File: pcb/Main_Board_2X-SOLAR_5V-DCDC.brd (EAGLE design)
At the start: 77.1 x 38.9 mm, 74 parts, among them CN5 USBA_FEMALE, M3AB FDMC8030, T2 MMUN2133LT1G, U1 LTC4015EUHFPBFQFN-38_UHF-M, U3 TPS61090RSAR, X1 6V_PV

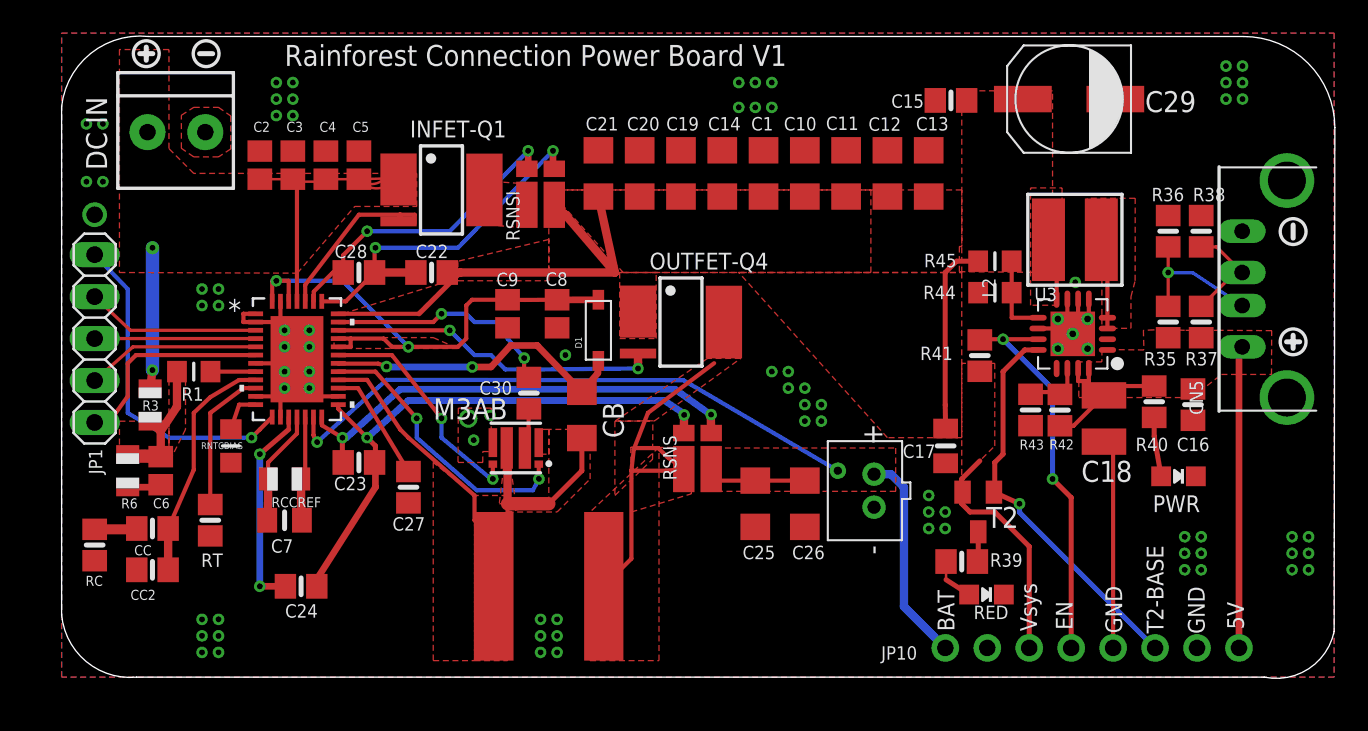
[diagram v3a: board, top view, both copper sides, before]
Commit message: Updated schematic and board layout for V1
Added jumper for VIN and updated footprint for 8030 package
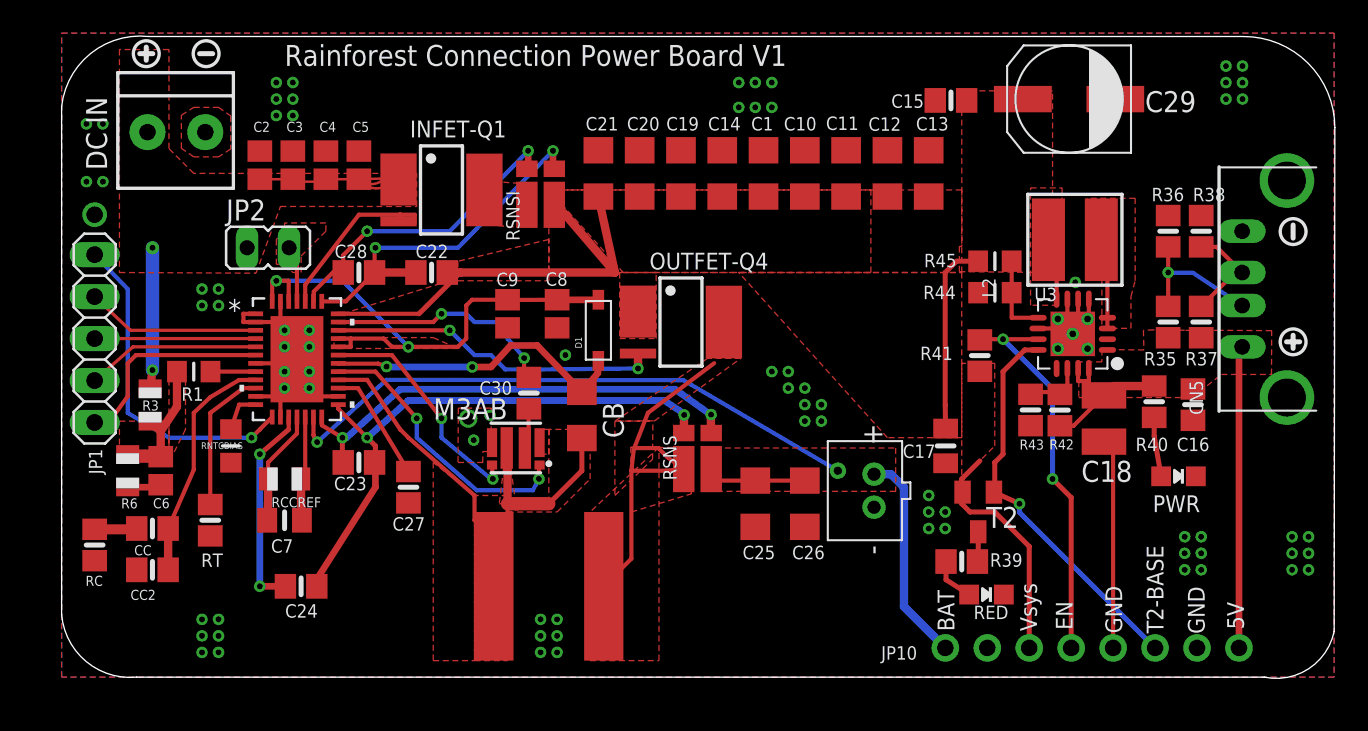
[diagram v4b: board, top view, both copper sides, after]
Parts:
- added JP2: (no value), jumper:JP1
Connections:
- new net N$12: JP2.2, U1.35
- net VIN: now also JP2.1; no longer U1.35
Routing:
- net VIN: track 29.1 -> 21.9 mm
- net N$12: track 0.00 -> 3.45 mm
- added copper zone on layer 1, net N$12
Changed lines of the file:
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@@
 <attribute name="PRICE" value="0.98 USD" x="23" y="29.5" size="1.778" layer="27" rot="R270" display="off"/>
 </element>
+<element name="JP2" library="jumper" library_urn="urn:adsk.eagle:library:252" package="JP1" package3d_urn="urn:adsk.eagle:package:15455/1" value="" x="12.5" y="26" rot="R270"/>
 </elements>
 <signals>
@@
 <wire x1="63.080540625" y1="17.028540625" x2="63.112" y2="17.06" width="0.254" layer="1"/>
 <wire x1="63.112" y1="17.06" x2="63.678" y2="17.626" width="0.254" layer="1"/>
-<wire x1="66.152" y1="17.626" x2="63.678" y2="17.626" width="0.254" layer="1"/>
+<wire x1="66.152" y1="17.626" x2="63.678" y2="17.626" width="0.508" layer="1"/>
 <wire x1="62.196" y1="17.927328125" x2="62.196" y2="18.686" width="0.254" layer="1"/>
 <wire x1="62.196" y1="17.927328125" x2="62.196" y2="17.028540625" width="0.254" layer="1"/>
@@
 <contactref element="C4" pad="1"/>
 <contactref element="C5" pad="1"/>
-<contactref element="U1" pad="35"/>
 <contactref element="X1" pad="1"/>
 <contactref element="R3" pad="2"/>
@@
 <vertex x="3.5" y="38"/>
 <vertex x="3.5" y="24.5"/>
-<vertex x="14.27" y="24.46"/>
-<vertex x="17.75" y="28.5"/>
+<vertex x="11.77" y="24.46"/>
+<vertex x="13.25" y="28.5"/>
 <vertex x="21.5" y="28.5"/>
 <vertex x="21.5" y="30.5"/>
@@
 <vertex x="6.5" y="32"/>
 </polygon>
-<wire x1="14.25" y1="22.7532" x2="14.25" y2="29.9" width="0.254" layer="1"/>
 <wire x1="14.425" y1="30.075" x2="14.25" y2="29.9" width="0.254" layer="1"/>
 <wire x1="19.541975" y1="30.191975" x2="18" y2="30.15" width="0.1524" layer="1"/>
@@
 <wire x1="5.5" y1="18.59" x2="5.36" y2="17.48" width="0.508" layer="1"/>
 <contactref element="INFET-Q1" pad="1-3"/>
+<contactref element="JP2" pad="1"/>
 </signal>
 <signal name="SYS">
@@
 <via x="28.9" y="12" extent="1-16" drill="0.35"/>
 <wire x1="28.9" y1="12" x2="28.89" y2="12.39" width="0.254" layer="1"/>
-<wire x1="28.89" y1="12.39" x2="28.89" y2="12.8971" width="0.254" layer="1"/>
+<wire x1="28.89" y1="12.39" x2="28.94" y2="12.845" width="0.254" layer="1"/>
 <wire x1="16.7532" y1="18.5" x2="19" y2="18.5" width="0.254" layer="1"/>
 <wire x1="19" y1="18.5" x2="21.5" y2="15.67" width="0.254" layer="1"/>
@@
 <contactref element="M3AB" pad="8"/>
 <via x="26.11" y="12" extent="1-16" drill="0.35"/>
-<wire x1="26.11" y1="12.8971" x2="26.11" y2="12" width="0.254" layer="1"/>
+<wire x1="26.06" y1="12.845" x2="26.11" y2="12" width="0.254" layer="1"/>
 <wire x1="16.7532" y1="19.5" x2="20" y2="19.5" width="0.254" layer="1"/>
 <wire x1="20" y1="19.5" x2="23" y2="15.67" width="0.254" layer="1"/>
@@
 <contactref element="R38" pad="1"/>
 <contactref element="CN5" pad="D+"/>
-<wire x1="69" y1="22.45" x2="71.05" y2="24.5" width="0.2" layer="1"/>
-<wire x1="71.05" y1="24.5" x2="71.48" y2="24.5" width="0.2" layer="1"/>
-<wire x1="71.48" y1="24.5" x2="69.93" y2="26.05" width="0.2" layer="1"/>
-<wire x1="69.93" y1="26.05" x2="69" y2="26.05" width="0.2" layer="1"/>
+<wire x1="69" y1="22.45" x2="71.05" y2="24.5" width="0.254" layer="1"/>
+<wire x1="71.05" y1="24.5" x2="71.48" y2="24.5" width="0.254" layer="1"/>
+<wire x1="71.48" y1="24.5" x2="69.93" y2="26.05" width="0.254" layer="1"/>
+<wire x1="69.93" y1="26.05" x2="69" y2="26.05" width="0.254" layer="1"/>
 </signal>
 <signal name="D-1">
@@
 <contactref element="R36" pad="1"/>
 <contactref element="CN5" pad="D-"/>
-<wire x1="71.48" y1="22.5" x2="68.4975" y2="24.4825" width="0.2" layer="16"/>
-<wire x1="66.947296875" y1="24.4825" x2="68.4975" y2="24.4825" width="0.2" layer="16"/>
+<wire x1="71.48" y1="22.5" x2="68.4975" y2="24.4825" width="0.254" layer="16"/>
+<wire x1="66.947296875" y1="24.4825" x2="68.4975" y2="24.4825" width="0.254" layer="16"/>
 <via x="67" y="24.5" extent="1-16" drill="0.35"/>
 <wire x1="66.947296875" y1="24.4825" x2="66.8460375" y2="24.4825" width="0.2" layer="16"/>
-<wire x1="67" y1="24.5" x2="67" y2="26.05" width="0.2" layer="1"/>
-<wire x1="67" y1="22.45" x2="67" y2="24.5" width="0.2" layer="1"/>
+<wire x1="67" y1="24.5" x2="67" y2="26.05" width="0.254" layer="1"/>
+<wire x1="67" y1="22.45" x2="67" y2="24.5" width="0.254" layer="1"/>
 <wire x1="67" y1="24.5" x2="66.9825" y2="24.4825" width="0.2" layer="16"/>
 <wire x1="66.9825" y1="24.4825" x2="66.947296875" y2="24.4825" width="0.2" layer="16"/>
@@
 <contactref element="R39" pad="1"/>
 <contactref element="RED" pad="A"/>
-<wire x1="53.55" y1="7" x2="53.55" y2="5.9" width="0.1524" layer="1"/>
+<wire x1="53.55" y1="7" x2="53.55" y2="5.9" width="0.3048" layer="1"/>
 <wire x1="53.55" y1="5.9" x2="54.95" y2="5" width="0.3048" layer="1"/>
 </signal>
@@
 <wire x1="34.9001875" y1="18.68830625" x2="34.9" y2="19.06811875" width="0.508" layer="1"/>
 <wire x1="34.9" y1="19.06811875" x2="34.9" y2="19.595" width="0.508" layer="1"/>
+</signal>
+<signal name="N$12">
+<contactref element="U1" pad="35"/>
+<contactref element="JP2" pad="2"/>
+<wire x1="14.25" y1="22.7532" x2="14.25" y2="25.52" width="0.254" layer="1"/>
+<wire x1="14.25" y1="25.52" x2="13.77" y2="26" width="0.254" layer="1"/>
+<polygon width="0.1524" layer="1" thermals="no">
+<vertex x="14.5" y="24.5"/>
+<vertex x="14.5" y="25.5"/>
+<vertex x="16" y="27"/>
+<vertex x="16" y="27.5"/>
+<vertex x="13.5" y="27.5"/>
+<vertex x="13.5" y="27"/>
+<vertex x="13" y="26.5"/>
+<vertex x="13" y="25"/>
+<vertex x="13.5" y="25"/>
+<vertex x="14" y="24.5"/>
+</polygon>
 </signal>
 </signals>
@@
 with this version.
 </note>
+<note version="8.3" severity="warning">
+Since Version 8.3, EAGLE supports URNs for individual library
+assets (packages, symbols, and devices). The URNs of those assets
+will not be understood (or retained) with this version.
+</note>
+<note version="8.3" severity="warning">
+Since Version 8.3, EAGLE supports the association of 3D packages
+with devices in libraries, schematics, and board files. Those 3D
+packages will not be understood (or retained) with this version.
+</note>
 </compatibility>

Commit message: OSH print V1 P2
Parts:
- added C31: 2.2 nF, adafruit:C0805
- moved C1 1.00 mm to (43.5, 30.5)
- moved C10 1.00 mm to (46.0, 30.5)
- moved C11 1.00 mm to (48.5, 30.5)
- moved C12 1.00 mm to (51.0, 30.5)
- moved C13 1.00 mm to (53.5, 30.5)
- moved C14 1.00 mm to (41.0, 30.5)
- moved C19 1.00 mm to (38.5, 30.5)
- moved C20 1.00 mm to (36.0, 30.5)
- moved C21 1.00 mm to (33.5, 30.5)
- moved C30 0.99 mm to (27.3, 17.3), turned to 180 degrees
- moved LED4 0.51 mm to (68.0, 12.5)
- moved C6 0.50 mm to (6.50, 12.5)
- moved R6 0.50 mm to (4.50, 12.5)
- moved RSNSI 0.50 mm to (29.5, 29.0)
- moved RT 0.50 mm to (9.00, 9.00)
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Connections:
- net N$5: now also C6.1
- net UVCLFB: now also C31.2; no longer C6.1
- net VIN: now also C31.1
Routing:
- net N$5: track 2.73 -> 9.04 mm
- net VIN: track 21.9 -> 27.3 mm
- net N$4: track 2.45 -> 4.79 mm
- net GND: track 42.8 -> 40.7 mm
- net N$2: track 14.5 -> 16.3 mm
- net UVCLFB: track 8.37 -> 10.0 mm
- net CSPM5: track 12.6 -> 13.5 mm
- net RT: track 8.80 -> 9.30 mm
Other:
- board size 77.1 x 38.9 mm -> 77.1 x 38.8 mm
- board text added: "P2"

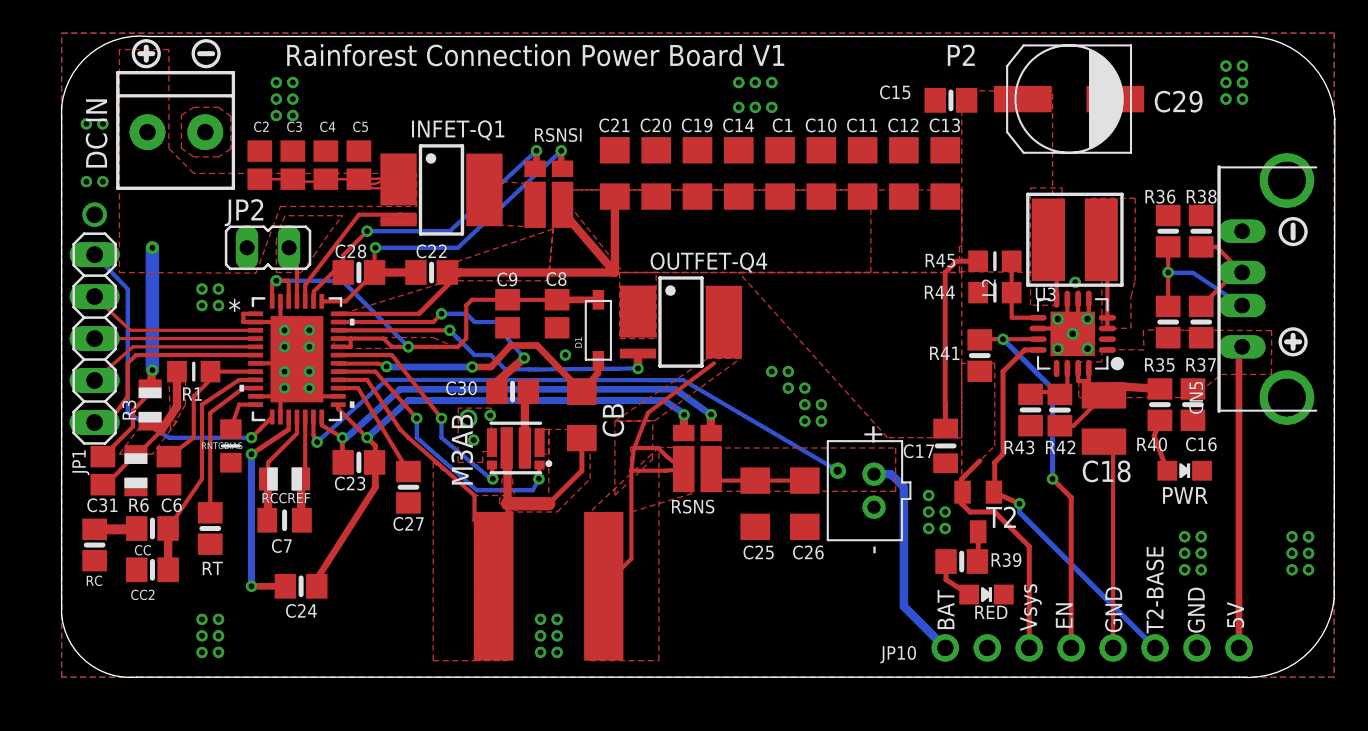
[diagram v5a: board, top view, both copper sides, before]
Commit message: Fixed NTC resistor routing
Added 10k NTC resistor to NTC pin and added INTVCC output to jumpers. Updated silkscreens for easier reading
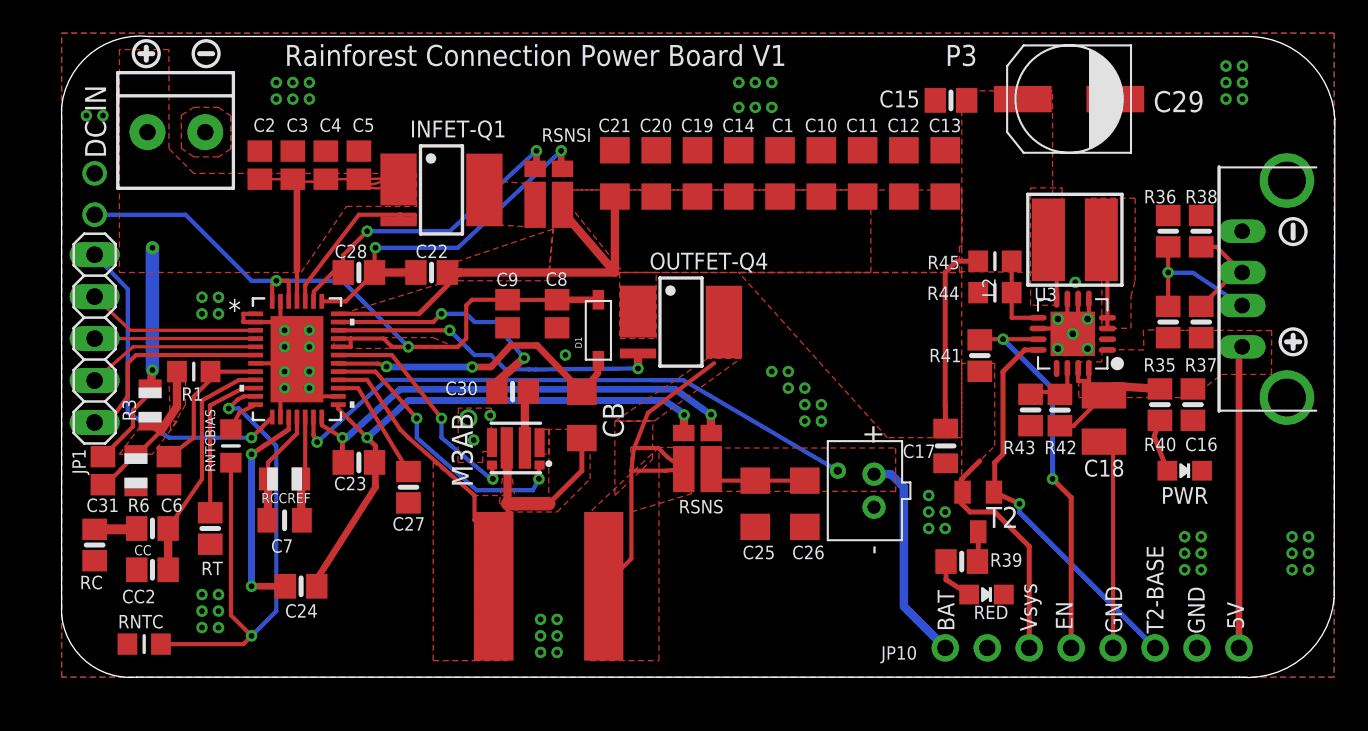
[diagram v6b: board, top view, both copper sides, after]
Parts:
- removed JP2: (no value), jumper:JP1
- added RNTC: 10k, microbuilder:_0805MP
- C31: value 2.2 nF -> 2200 pF
- renumbered U$4 to L1
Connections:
- net GND: now also RNTC.1; no longer RNTCBIAS.1, U1.11
- net N$12: now also RNTC.2, RNTCBIAS.1, U1.11; no longer JP2.2, U1.35
- net VIN: now also U1.35; no longer JP2.1
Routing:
- net N$12: track 3.45 -> 34.5 mm, vias 0 -> 2
- net INTVCC: track 33.0 -> 45.7 mm, vias 2 -> 3
- net VIN: track 27.3 -> 35.6 mm
- net GND: track 40.7 -> 39.4 mm, vias 77 -> 75
- removed copper zone on layer 1, net N$12
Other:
- board text added: "DVCC"
- board text added: "EQ"
- board text added: "INTVCC"
- board text added: "P3"
- board text added: "SCL"
- board text added: "SDA"
- board text added: "SMBALERT"
- board text removed: "P2"

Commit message: Sentinel Board V1P3
Updated silkscreen and added MPPT switch to allow for logic level/pin selection for MPPT instead of i2c only.
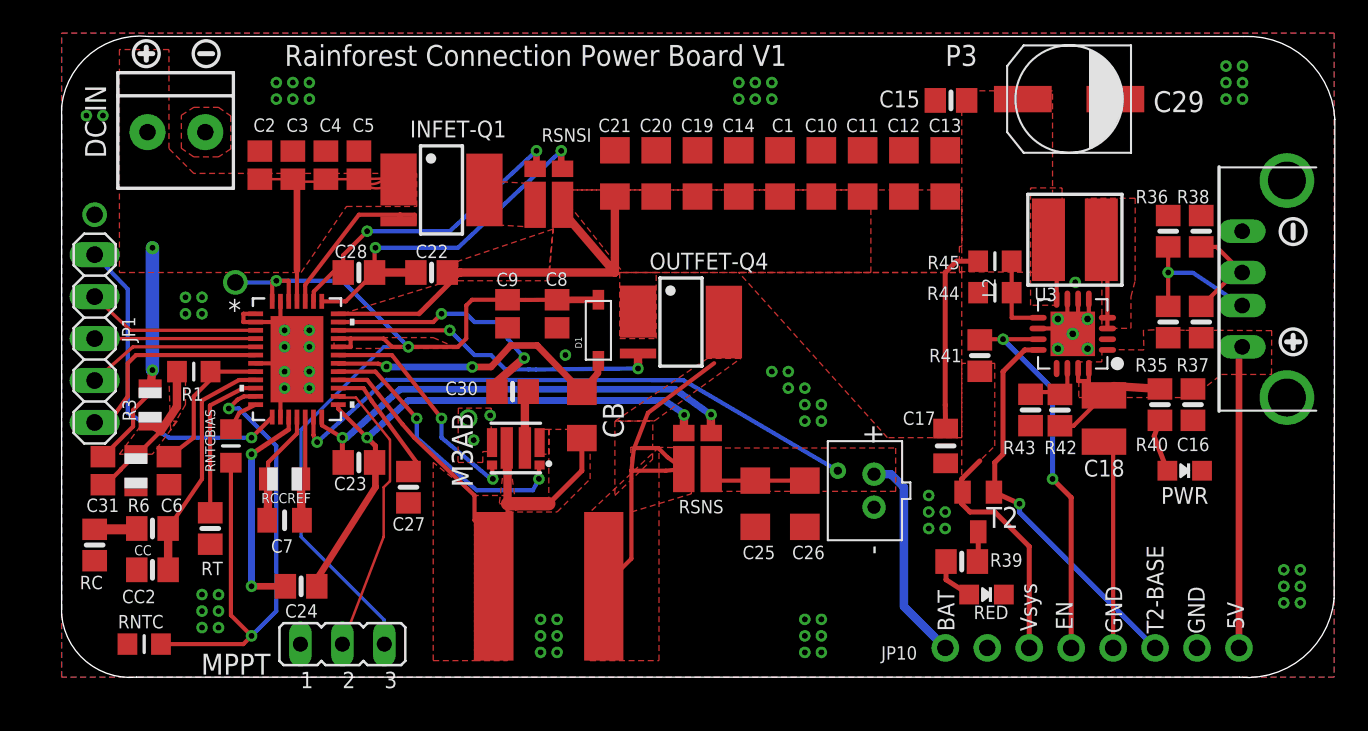
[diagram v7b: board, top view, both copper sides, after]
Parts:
- added MPPT: (no value), jumper:JP2
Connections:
- new net MPPT: MPPT.2, U1.21
- net GND: now also MPPT.1; no longer U1.21
- net INTVCC: now also MPPT.3
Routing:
- net MPPT: track 0.00 -> 17.4 mm
- net INTVCC: track 45.7 -> 59.2 mm
- net GND: track 39.4 -> 37.7 mm
- net 2P5VCC: track 7.10 -> 7.82 mm

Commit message: Sentinel V1 P4 updated layout
Fixed schematic and board layout for easier assembly and corrected connection to M3AB NMOS pair.
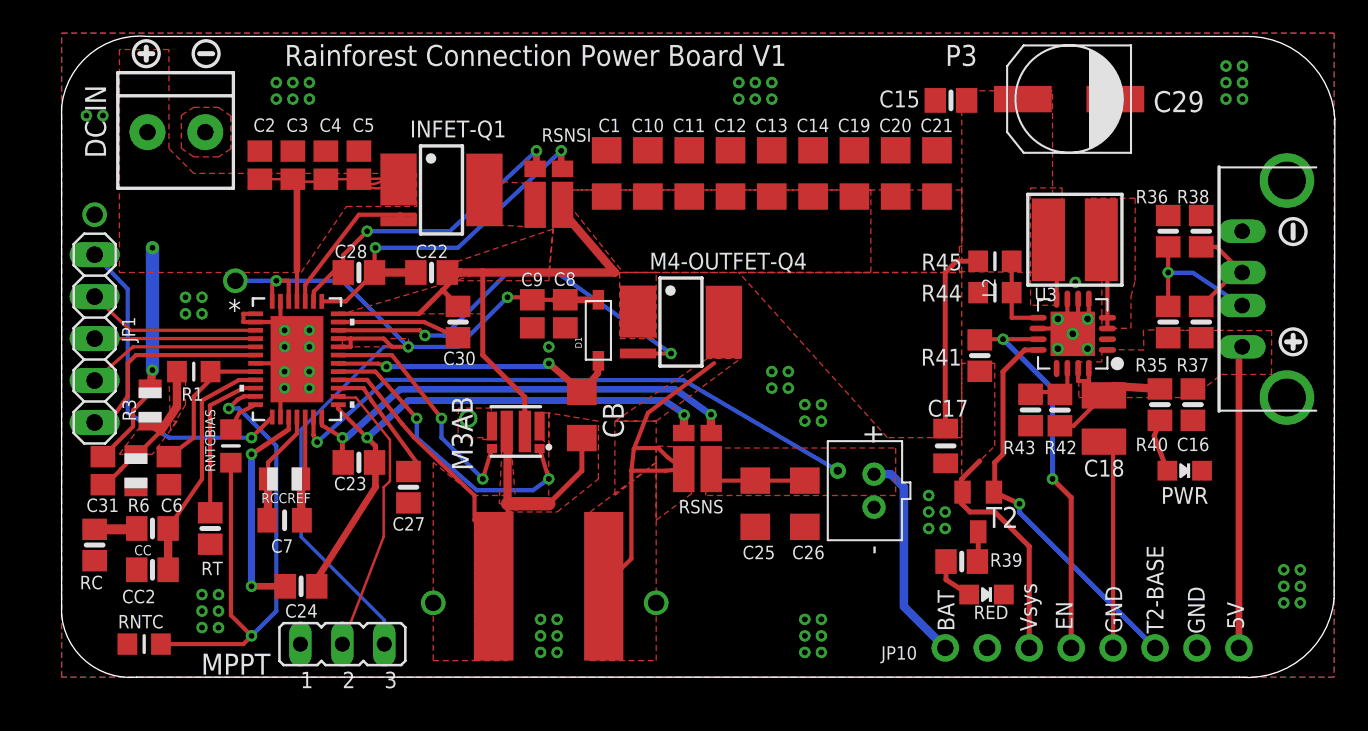
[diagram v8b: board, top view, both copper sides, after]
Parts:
- moved C21 19.5 mm to (53.0, 30.5)
- moved C20 14.5 mm to (50.5, 30.5)
- moved C1 10.5 mm to (33.0, 30.5)
- moved C10 10.5 mm to (35.5, 30.5)
- moved C11 10.5 mm to (38.0, 30.5)
- moved C12 10.5 mm to (40.5, 30.5)
- moved C13 10.5 mm to (43.0, 30.5)
- moved C19 9.50 mm to (48.0, 30.5)
- moved C30 5.35 mm to (24.0, 21.5), turned to 270 degrees
- moved C14 4.50 mm to (45.5, 30.5)
- moved C9 1.50 mm to (28.5, 22.0)
- moved M3AB 1.00 mm to (27.5, 14.9)
- moved C8 0.50 mm to (30.5, 22.0)
- renumbered OUTFET-Q4 to M4-OUTFET-Q4
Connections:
- net N$10 renamed OUTFET
- net N$13 renamed BOOST
- net N$2 renamed SYSM5
- net OUTFET_M4_SOURCE renamed OUTFET_M4_BAT
- removed net N$4: C30.1, M3AB.10
- net SYS: now also C30.1, M3AB.10
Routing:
- net SYSM5: track 16.3 -> 7.46 mm, vias 2 -> 0
- net SYS: track 58.6 -> 66.1 mm
- net OUTFET: track 20.0 -> 25.4 mm
- net N$4: track 4.79 -> 0.00 mm
- net SW_LTC: track 31.5 -> 33.2 mm, vias 0 -> 1
- net TG: track 17.0 -> 18.5 mm
- net BOOST: track 18.8 -> 17.8 mm
- net INTVCC: track 59.2 -> 60.0 mm, vias 3 -> 4
- net BG: track 14.1 -> 14.7 mm
- net OUTFET_M4_BAT: vias 0 -> 1
- net GND: vias 75 -> 73
